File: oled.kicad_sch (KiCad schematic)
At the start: 4 parts, among them J2 ST7789 oled 128x64, J23 conector oled ST1306 128x32

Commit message: feat: PCB layout updates, schematic changes, fp-lib-table config
- cnc_pic32.kicad_pcb: component repositioning, board outline, text formatting
- cnc_pic32.kicad_prl/pro: project settings updates
- fp-lib-table: add Library path to Library.pretty
- mcu.kicad_sch: PIC32 pin configuration updates
- zigbee.kicad_sch: MRF24J40 module updates
- oscilator.kicad_sch: crystal configuration
- power.kicad_sch/power_ft232.kicad_sch: power supply updates
- oled.kicad_sch: OLED display connections
- idc.kicad_sch: IDC connector updates
- osc_ft232.kicad_sch: FT232 crystal
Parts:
- J22: renamed from J2; value ST7789 oled 128x64 -> Adafruit ST7789; footprint kiC:Adafruit_SSD1306_No_Mounting_Holes_pads -> Library:Adafruit_SSD1306_No_Mounting_Holes_pads
- renumbered J23 to J21, R42 to R31, R41 to R32
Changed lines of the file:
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@@
 		(dnp no)
 		(fields_autoplaced yes)
-		(property "Reference" "J23"
+		(property "Reference" "J21"
 			(at 153.67 78.7399 0)
 			(show_name no)
@@
 			(project "cnc_pic32"
 				(path "/13dbfc1f-be47-44ca-9042-3d6a9a657d7d/907034bd-da52-4a91-8e77-55c555a9b713"
-					(reference "J23")
+					(reference "J21")
 					(unit 1)
 				)
@@
 		(dnp no)
 		(fields_autoplaced yes)
-		(property "Reference" "#PWR044"
+		(property "Reference" "#PWR068"
 			(at 210.82 81.28 0)
 			(hide yes)
@@
 			(project "cnc_pic32"
 				(path "/13dbfc1f-be47-44ca-9042-3d6a9a657d7d/907034bd-da52-4a91-8e77-55c555a9b713"
-					(reference "#PWR044")
+					(reference "#PWR068")
 					(unit 1)
 				)
@@
 		(in_pos_files yes)
 		(dnp no)
-		(property "Reference" "J2"
+		(property "Reference" "J22"
 			(at 189.865 69.85 0)
 			(show_name no)
@@
 			)
 		)
-		(property "Value" "ST7789 oled 128x64"
+		(property "Value" "Adafruit ST7789"
 			(at 180.086 73.152 0)
 			(show_name no)
@@
 			)
 		)
-		(property "Footprint" "kiC:Adafruit_SSD1306_No_Mounting_Holes_pads"
+		(property "Footprint" "Library:Adafruit_SSD1306_No_Mounting_Holes_pads"
 			(at 189.23 82.55 0)
 			(hide yes)
@@
 			(project "cnc_pic32"
 				(path "/13dbfc1f-be47-44ca-9042-3d6a9a657d7d/907034bd-da52-4a91-8e77-55c555a9b713"
-					(reference "J2")
+					(reference "J22")
 					(unit 1)
 				)
@@
 		(dnp no)
 		(fields_autoplaced yes)
-		(property "Reference" "#PWR068"
+		(property "Reference" "#PWR065"
 			(at 119.38 80.01 0)
 			(hide yes)
@@
 			(project "cnc_pic32"
 				(path "/13dbfc1f-be47-44ca-9042-3d6a9a657d7d/907034bd-da52-4a91-8e77-55c555a9b713"
-					(reference "#PWR068")
+					(reference "#PWR065")
 					(unit 1)
 				)
@@
 		(dnp no)
 		(fields_autoplaced yes)
-		(property "Reference" "R42"
+		(property "Reference" "R31"
 			(at 92.71 110.49 0)
 			(show_name no)
@@
 			(project "cnc_pic32"
 				(path "/13dbfc1f-be47-44ca-9042-3d6a9a657d7d/907034bd-da52-4a91-8e77-55c555a9b713"
-					(reference "R42")
+					(reference "R31")
 					(unit 1)
 				)
@@
 		(dnp no)
 		(fields_autoplaced yes)
-		(property "Reference" "#PWR069"
+		(property "Reference" "#PWR066"
 			(at 125.73 72.39 0)
 			(hide yes)
@@
 			(project "cnc_pic32"
 				(path "/13dbfc1f-be47-44ca-9042-3d6a9a657d7d/907034bd-da52-4a91-8e77-55c555a9b713"
-					(reference "#PWR069")
+					(reference "#PWR066")
 					(unit 1)
 				)
@@
 		(dnp no)
 		(fields_autoplaced yes)
-		(property "Reference" "#PWR070"
+		(property "Reference" "#PWR063"
 			(at 90.17 111.76 0)
 			(hide yes)
@@
 			(project "cnc_pic32"
 				(path "/13dbfc1f-be47-44ca-9042-3d6a9a657d7d/907034bd-da52-4a91-8e77-55c555a9b713"
-					(reference "#PWR070")
+					(reference "#PWR063")
 					(unit 1)
 				)
@@
 		(dnp no)
 		(fields_autoplaced yes)
-		(property "Reference" "R41"
+		(property "Reference" "R32"
 			(at 106.68 110.49 0)
 			(show_name no)
@@
 			(project "cnc_pic32"
 				(path "/13dbfc1f-be47-44ca-9042-3d6a9a657d7d/907034bd-da52-4a91-8e77-55c555a9b713"
-					(reference "R41")
+					(reference "R32")
 					(unit 1)
 				)
@@
 		(dnp no)
 		(fields_autoplaced yes)
-		(property "Reference" "#PWR071"
+		(property "Reference" "#PWR064"
 			(at 104.14 111.76 0)
 			(hide yes)
@@
 			(project "cnc_pic32"
 				(path "/13dbfc1f-be47-44ca-9042-3d6a9a657d7d/907034bd-da52-4a91-8e77-55c555a9b713"
-					(reference "#PWR071")
-					(unit 1)
-				)
+					(reference "#PWR064")
+					(unit 1)
+				)

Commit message: feat: integrate zigbee sheet + R 0603→0805 footprint update
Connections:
- net RG7: now reaches J21.5 (Pin_5)
- net RG8: now reaches J21.6 (Pin_6)
- net RG0: now reaches J22.5 (Pin_5)
- net RG1: now reaches J22.6 (Pin_6)
- net RG6: now reaches J22.7 (Pin_7)
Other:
- moved on the sheet: R31
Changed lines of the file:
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@@
 	(hierarchical_label "scl"
 		(shape input)
-		(at 90.17 115.57 180)
+		(at 90.17 105.41 180)
 		(effects
 			(font
@@
 		)
 	)
+	(hierarchical_label "RG6"
+		(shape input)
+		(at 194.31 90.17 0)
+		(effects
+			(font
+				(size 1.27 1.27)
+			)
+			(justify left)
+		)
+	)
 	(hierarchical_label "scl"
 		(shape input)
@@
 		)
 	)
+	(hierarchical_label "RG1"
+		(shape input)
+		(at 194.31 87.63 0)
+		(effects
+			(font
+				(size 1.27 1.27)
+			)
+			(justify left)
+		)
+	)
 	(hierarchical_label "sda"
 		(shape input)
 		(at 90.17 118.11 180)
+		(effects
+			(font
+				(size 1.27 1.27)
+			)
+			(justify right)
+		)
+	)
+	(hierarchical_label "RG0"
+		(shape input)
+		(at 194.31 85.09 0)
+		(effects
+			(font
+				(size 1.27 1.27)
+			)
+			(justify left)
+		)
+	)
+	(hierarchical_label "RG8"
+		(shape input)
+		(at 146.05 86.36 180)
+		(effects
+			(font
+				(size 1.27 1.27)
+			)
+			(justify right)
+		)
+	)
+	(hierarchical_label "RG7"
+		(shape input)
+		(at 146.05 83.82 180)
 		(effects
 			(font
@@
 		(in_pos_files yes)
 		(dnp no)
-		(fields_autoplaced yes)
 		(property "Reference" "J21"
-			(at 153.67 78.7399 0)
+			(at 139.954 66.802 0)
 			(show_name no)
 			(do_not_autoplace no)
@@
 		)
 		(property "Value" "conector oled ST1306 128x32"
-			(at 153.67 81.2799 0)
+			(at 125.476 70.358 0)
 			(show_name no)
 			(do_not_autoplace no)
@@
 		)
 		(property "Value" "Adafruit ST7789"
-			(at 180.086 73.152 0)
+			(at 195.072 65.786 0)
 			(show_name no)
 			(do_not_autoplace no)
@@
 	(symbol
 		(lib_id "Device:R")
-		(at 90.17 111.76 0)
+		(at 90.17 101.6 0)
 		(unit 1)
 		(body_style 1)
@@
 		(fields_autoplaced yes)
 		(property "Reference" "R31"
-			(at 92.71 110.49 0)
+			(at 92.71 100.33 0)
 			(show_name no)
 			(do_not_autoplace no)
@@
 		)
 		(property "Value" "1k"
-			(at 92.71 113.03 0)
+			(at 92.71 102.87 0)
 			(show_name no)
 			(do_not_autoplace no)
@@
 		)
 		(property "Footprint" "Resistor_SMD:R_0805_2012Metric"
-			(at 88.392 111.76 90)
+			(at 88.392 101.6 90)
 			(hide yes)
 			(show_name no)
@@
 		)
 		(property "Datasheet" ""
-			(at 90.17 111.76 0)
+			(at 90.17 101.6 0)
 			(hide yes)
 			(show_name no)
@@
 		)
 		(property "Description" ""
-			(at 90.17 111.76 0)
+			(at 90.17 101.6 0)
 			(show_name no)
 			(do_not_autoplace no)
@@
 	(symbol
 		(lib_id "power:+3.3V")
-		(at 90.17 107.95 0)
+		(at 90.17 97.79 0)
 		(unit 1)
 		(body_style 1)
@@
 		(fields_autoplaced yes)
 		(property "Reference" "#PWR063"
-			(at 90.17 111.76 0)
+			(at 90.17 101.6 0)
 			(hide yes)
 			(show_name no)
@@
 		)
 		(property "Value" "+3.3V"
-			(at 90.17 102.87 0)
+			(at 90.17 92.71 0)
 			(show_name no)
 			(do_not_autoplace no)
@@
 		)
 		(property "Footprint" ""
-			(at 90.17 107.95 0)
+			(at 90.17 97.79 0)
 			(hide yes)
 			(show_name no)
@@
 		)
 		(property "Datasheet" ""
-			(at 90.17 107.95 0)
+			(at 90.17 97.79 0)
 			(hide yes)
 			(show_name no)
@@
 		)
 		(property "Description" "Power symbol creates a global label with name \"+3.3V\""
-			(at 90.17 107.95 0)
-			(hide yes)
-			(show_name no)
+			(at 90.17 97.79 0)
+			(hide yes)
+			(show_name no)

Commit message: feat: add orphaned PCB components to schematics - R4/R5 MCU, R41/R42 OLED, C37/C38 power
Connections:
- net RG7: now also J21.4 (Pin_4); no longer J21.5 (Pin_5)
- net scl: now also J21.5 (Pin_5); no longer J21.3 (Pin_3)
- net sda: now also J21.3 (Pin_3); no longer J21.4 (Pin_4)
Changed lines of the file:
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@@
 	(hierarchical_label "sda"
 		(shape input)
-		(at 146.05 81.28 180)
+		(at 146.05 78.74 180)
 		(effects
 			(font
@@
 	(hierarchical_label "scl"
 		(shape input)
-		(at 146.05 78.74 180)
+		(at 146.05 83.82 180)
 		(effects
 			(font
@@
 	(hierarchical_label "RG7"
 		(shape input)
-		(at 146.05 83.82 180)
+		(at 146.05 81.28 180)
 		(effects
 			(font

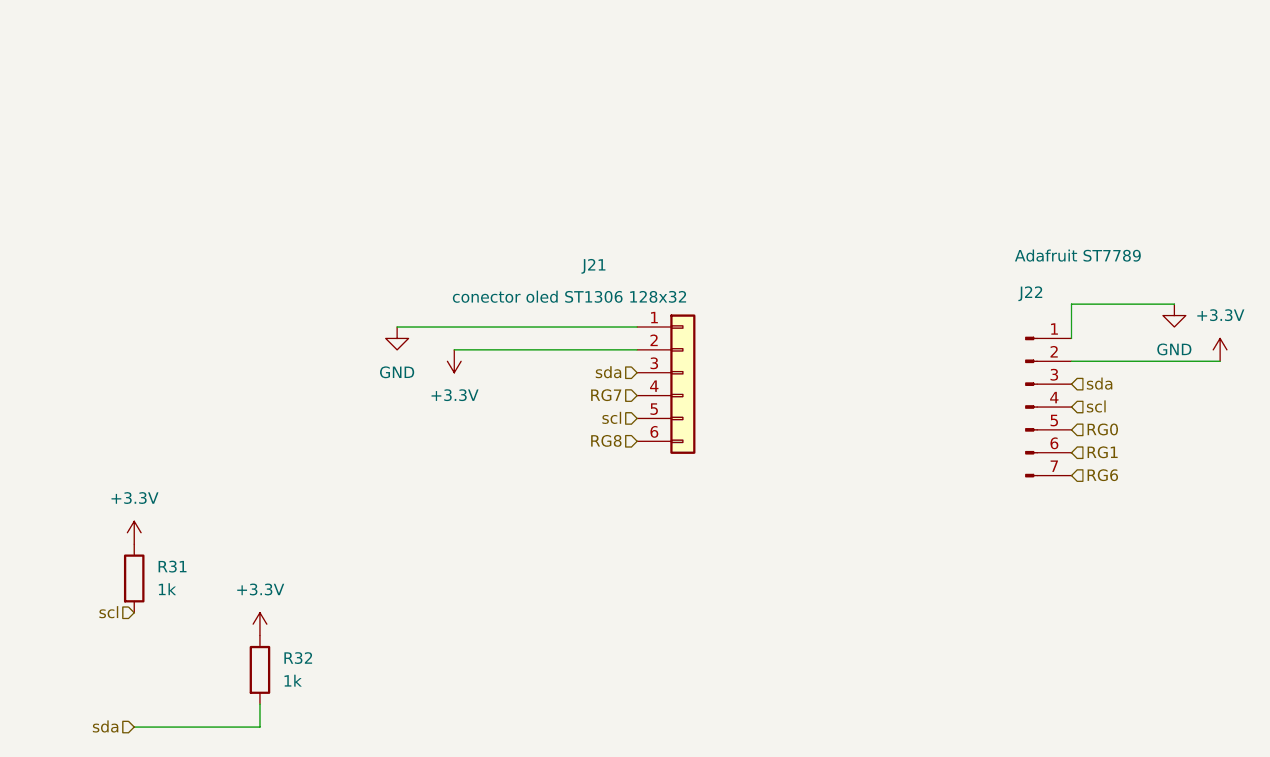
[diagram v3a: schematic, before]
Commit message: feat: 2-layer stackup, bus net class and schematic cleanup
PCB / project
- Reduce board from 4 layers to 2 (F.Cu / B.Cu) for cheaper fabrication
- Add "bus" net class and reorder net class priorities (bus 0, usb_differential 1, ...)

Schematics
- usb_conector_Ft232: add D+ / D-- labels on the USB mini-B data pair
- ft232: add 10K pull-ups, 100nf decoupling and test points on +3.3VA
- tp_ft232: remove solder jumpers JP1/JP2 (TX_Rpi / RX_Rpi now direct)
- Usb_pic32: add C38 100nf decoupling on +5V
- oled: expand connector J25 from 7 to 8 pins
- mcu / idc / power / zigbee / buttons / cnc_pic32: annotation and net cleanup

docs
- Add USB-Mini-B pinout reference images
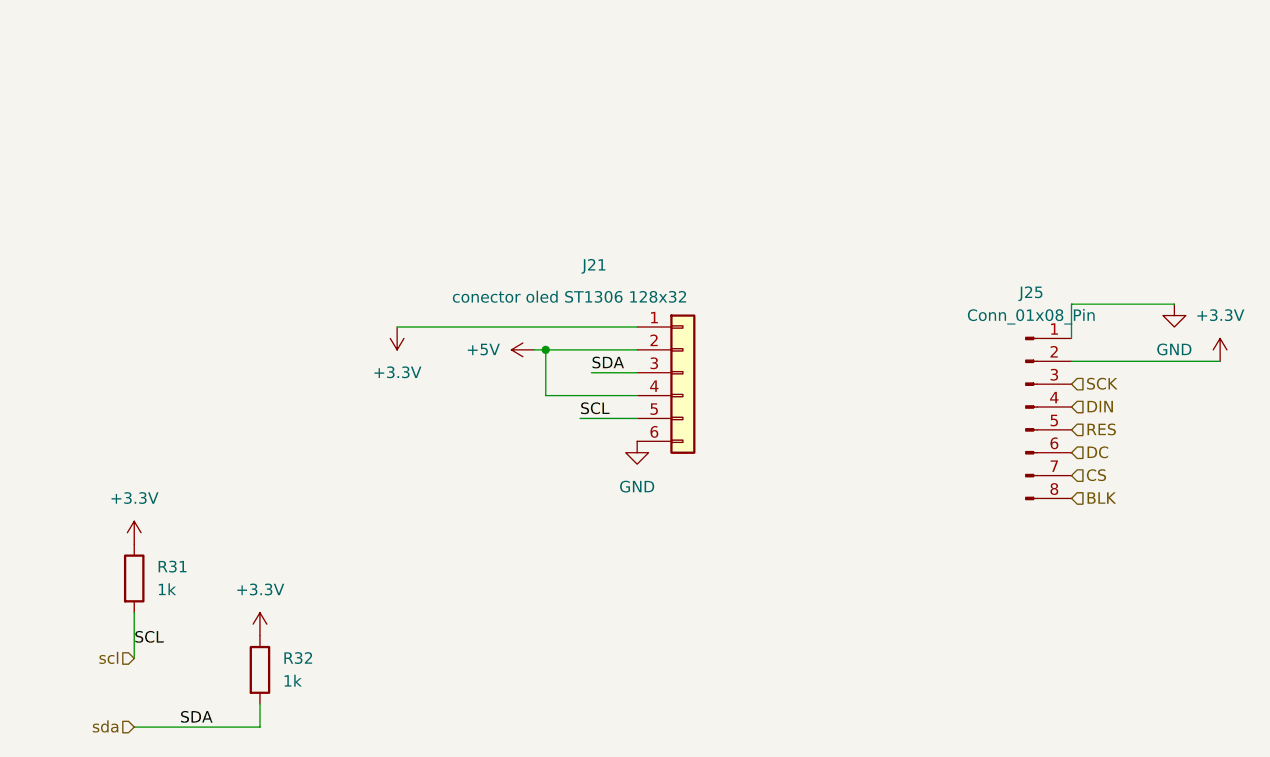
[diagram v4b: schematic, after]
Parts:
- removed J22: Adafruit ST7789, Library:Adafruit_SSD1306_No_Mounting_Holes_pads, symbol Connector:Conn_01x07_Pin
- added J25: Conn_01x08_Pin, Library:Adafruit_SSD1306_No_Mounting_Holes_pads, symbol Connector:Conn_01x08_Pin
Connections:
- net RG8 is gone; now on net GND: J21.6 (Pin_6)
- net +3.3V: now also J21.1 (Pin_1), J25.2 (Pin_2); no longer J21.2 (Pin_2)
- net GND: now also J25.1 (Pin_1); no longer J21.1 (Pin_1)
- net RG7 renamed +5V
- net +5V: now also J21.2 (Pin_2)
- new net BLK: J25.8 (Pin_8)
- new net CS: J25.7 (Pin_7)
- new net DC: J25.6 (Pin_6)
- new net DIN: J25.4 (Pin_4)
- new net RES: J25.5 (Pin_5)
- new net SCK: J25.3 (Pin_3)

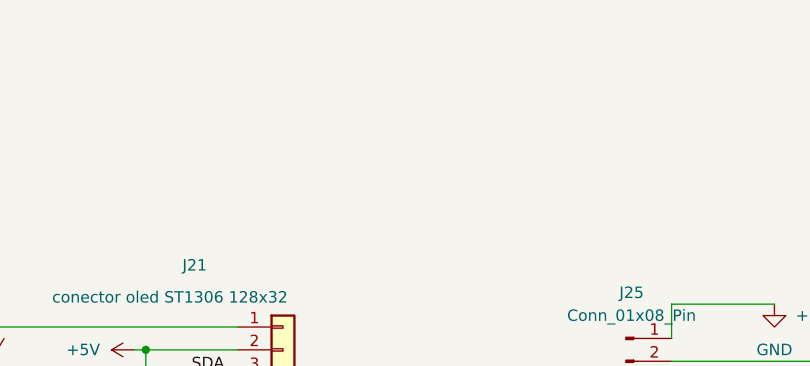
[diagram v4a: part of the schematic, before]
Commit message: feat: add MA240011 module sheet with labeled pins + Altium socket footprint
Esquemático
- Nueva hoja hija MA240011.kicad_sch (módulo PIC32 TQFP-100) referenciada
  desde la hoja MA240011 de mcu.kicad_sch
- mcu.kicad_sch: los 83 pines jerárquicos de MA240011 quedan rotulados con un
  label local del mismo nombre; 81 de ellos con un tramo de wire de 2.54 mm
  (un label solo no conecta a un pin de hoja) y RD4/RD5 sobre el wire existente
- mcu.kicad_sch: borde derecho del sheet 104.775 -> 106.68 mm y sus 41 pines,
  para quedar en grilla de 1.27 mm (evita 41 avisos endpoint_off_grid)
- ERC: 341 -> 158 violaciones; pin_not_connected 120 -> 39,
  isolated_pin_label 113 -> 10, endpoint_off_grid 6 -> 6
- power / zigbee / oled / pololu / cnc_pic32: pines MS1-MS3, conectores y
  anotacion de netnames

PCB
- Referencia de los 132 footprints a size 0.8 x 0.8 mm y thickness 0.12 mm
  (render_cache obsoleto eliminado para forzar el re-render)

Footprints
- lib/altium.pretty/MA240011_Socket_TQFP100_100pin.kicad_mod: zocalo adaptador
  de 100 pines TH pitch 1.27 mm convertido desde altium/Multimedia/MM20141127.PcbDoc
  (J4, patron MA240011); pads girados 90 grados sentido horario
- fp-lib-table: alta de la biblioteca "altium" (${KIPRJMOD}/lib/altium.pretty)

.gitignore
- Ignorar altium/, tmp/ y *.bkp (backups de KiCad)
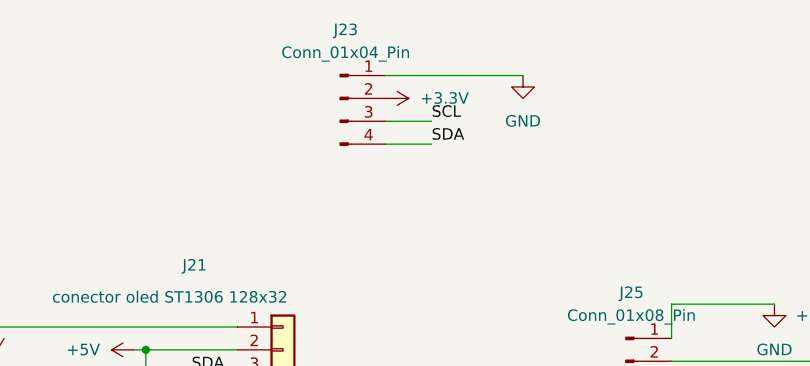
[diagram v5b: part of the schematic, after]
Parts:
- added J23: Conn_01x04_Pin, Connector_PinHeader_2.54mm:PinHeader_1x04_P2.54mm_Vertical, symbol Connector:Conn_01x04_Pin
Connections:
- net +3.3V: now also J23.2 (Pin_2)
- net GND: now also J23.1 (Pin_1)
- net scl: now also J23.3 (Pin_3)
- net sda: now also J23.4 (Pin_4)

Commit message: updated
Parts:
- J21: now left out of the parts list
- J23: value Conn_01x04_Pin -> OLED SSD1306; now left out of the parts list
- J25: footprint Library:Adafruit_SSD1306_No_Mounting_Holes_pads -> Connector_PinHeader_2.54mm:PinHeader_1x08_P2.54mm_Vertical; now left out of the parts list
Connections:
- net +5V: no longer names the net of J21.2 (Pin_2)
- net +5V: no longer J21.4 (Pin_4)
- net scl renamed scl_i2c_1
- net scl_i2c_1: no longer J21.5 (Pin_5)
- net sda renamed sda_i2c_1
- net sda_i2c_1: no longer J21.3 (Pin_3)
- new net scl_i2c_2: J21.5 (Pin_5)
- new net sda_i2c_2: J21.3 (Pin_3)
- no-connect marks 0 -> 2
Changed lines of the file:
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@@
 	(generator_version "10.0")
 	(paper "A4")
-	(junction
-		(at 135.89 76.2)
-		(diameter 0)
-		(color 0 0 0 0)
+	(no_connect
+		(at 146.05 76.2)
+	)
+	(no_connect
+		(at 146.05 81.28)
 	)
 	(wire
@@
 	(wire
 		(pts
-			(xy 135.89 81.28) (xy 135.89 76.2)
-		)
-		(stroke
-			(width 0)
-			(type default)
-		)
-	)
-	(wire
-		(pts
-			(xy 134.62 76.2) (xy 135.89 76.2)
-		)
-		(stroke
-			(width 0)
-			(type default)
-		)
-	)
-	(wire
-		(pts
 			(xy 167.64 53.34) (xy 162.56 53.34)
 		)
@@
 	(wire
 		(pts
-			(xy 146.05 81.28) (xy 135.89 81.28)
-		)
-		(stroke
-			(width 0)
-			(type default)
-		)
-	)
-	(wire
-		(pts
 			(xy 90.17 110.49) (xy 90.17 105.41)
 		)
@@
 		(pts
 			(xy 104.14 115.57) (xy 104.14 118.11)
-		)
-		(stroke
-			(width 0)
-			(type default)
-		)
-	)
-	(wire
-		(pts
-			(xy 135.89 76.2) (xy 146.05 76.2)
 		)
 		(stroke
@@
 		)
 	)
-	(label "SDA"
-		(at 140.97 78.74 0)
-		(effects
-			(font
-				(size 1.27 1.27)
-			)
-			(justify left bottom)
-		)
-	)
-	(label "SCL"
-		(at 139.7 83.82 0)
-		(effects
-			(font
-				(size 1.27 1.27)
-			)
-			(justify left bottom)
-		)
-	)
-	(hierarchical_label "scl"
+	(hierarchical_label "scl_i2c_1"
 		(shape input)
 		(at 90.17 110.49 180)
@@
 		)
 	)
+	(hierarchical_label "scl_i2c_2"
+		(shape input)
+		(at 139.7 83.82 180)
+		(effects
+			(font
+				(size 1.27 1.27)
+			)
+			(justify right)
+		)
+	)
+	(hierarchical_label "sda_i2c_2"
+		(shape input)
+		(at 140.97 78.74 180)
+		(effects
+			(font
+				(size 1.27 1.27)
+			)
+			(justify right)
+		)
+	)
 	(hierarchical_label "DIN"
 		(shape input)
@@
 		)
 	)
-	(hierarchical_label "sda"
+	(hierarchical_label "sda_i2c_1"
 		(shape input)
 		(at 90.17 118.11 180)
@@
 		(body_style 1)
 		(exclude_from_sim no)
-		(in_bom yes)
+		(in_bom no)
 		(on_board yes)
-		(in_pos_files yes)
+		(in_pos_files no)
 		(dnp no)
 		(property "Reference" "J21"
@@
 				(path "/13dbfc1f-be47-44ca-9042-3d6a9a657d7d/907034bd-da52-4a91-8e77-55c555a9b713"
 					(reference "J21")
-					(unit 1)
-				)
-			)
-		)
-	)
-	(symbol
-		(lib_id "power:+5V")
-		(at 134.62 76.2 90)
-		(unit 1)
-		(body_style 1)
-		(exclude_from_sim no)
-		(in_bom yes)
-		(on_board yes)
-		(in_pos_files yes)
-		(dnp no)
-		(fields_autoplaced yes)
-		(property "Reference" "#PWR082"
-			(at 138.43 76.2 0)
-			(hide yes)
-			(show_name no)
-			(do_not_autoplace no)
-			(effects
-				(font
-					(size 1.27 1.27)
-				)
-			)
-		)
-		(property "Value" "+5V"
-			(at 130.81 76.1999 90)
-			(show_name no)
-			(do_not_autoplace no)
-			(effects
-				(font
-					(size 1.27 1.27)
-				)
-				(justify left)
-			)
-		)
-		(property "Footprint" ""
-			(at 134.62 76.2 0)
-			(hide yes)
-			(show_name no)
-			(do_not_autoplace no)
-			(effects
-				(font
-					(size 1.27 1.27)
-				)
-			)
-		)
-		(property "Datasheet" ""
-			(at 134.62 76.2 0)
-			(hide yes)
-			(show_name no)
-			(do_not_autoplace no)
-			(effects
-				(font
-					(size 1.27 1.27)
-				)
-			)
-		)
-		(property "Description" "Power symbol creates a global label with name \"+5V\""
-			(at 134.62 76.2 0)
-			(hide yes)
-			(show_name no)
-			(do_not_autoplace no)
-			(effects
-				(font
-					(size 1.27 1.27)
-				)
-			)
-		)
-		(pin "1"
-		)
-		(instances
-			(project "cnc_pic32"
-				(path "/13dbfc1f-be47-44ca-9042-3d6a9a657d7d/907034bd-da52-4a91-8e77-55c555a9b713"
-					(reference "#PWR082")
 					(unit 1)
 				)
@@
 		(body_style 1)
 		(exclude_from_sim no)
-		(in_bom yes)
+		(in_bom no)
 		(on_board yes)
-		(in_pos_files yes)
+		(in_pos_files no)
 		(dnp no)
 		(fields_autoplaced yes)
@@
 			)
 		)
-		(property "Footprint" "Library:Adafruit_SSD1306_No_Mounting_Holes_pads"
+		(property "Footprint" "Connector_PinHeader_2.54mm:PinHeader_1x08_P2.54mm_Vertical"
 			(at 189.23 82.55 0)
 			(hide yes)
@@
 		(body_style 1)
 		(exclude_from_sim no)
-		(in_bom yes)
+		(in_bom no)
 		(on_board yes)
-		(in_pos_files yes)
+		(in_pos_files no)
 		(dnp no)
 		(fields_autoplaced yes)
@@
 			)
 		)
-		(property "Value" "Conn_01x04_Pin"
+		(property "Value" "OLED SSD1306"
 			(at 158.115 43.18 0)
 			(show_name no)
